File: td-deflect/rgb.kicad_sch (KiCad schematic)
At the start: 83 parts, among them J16 Conn_01x06_Male, J17 Conn_01x06_Male, J5 DB15_Female_HighDensity, J7 Conn_01x08_Male, Q14 BC847, Q15 BC847, Q16 BC847, SW1 SW_DIP_x04, U11 24LC08, U18 M51387P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

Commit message: more updates
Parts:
- removed C59: 0.1uF, Capacitor_SMD:C_0805_2012Metric_Pad1.15x1.40mm_HandSolder, symbol Device:C
- removed C60: 220uF, Capacitor_THT:CP_Radial_D8.0mm_P3.50mm, symbol Device:CP
- removed D6, D7, D8: BAT54S, Package_TO_SOT_SMD:SOT-23, symbol Diode:BAT54S
- removed Q14, Q15, Q16: BC847, Package_TO_SOT_SMD:SOT-23, symbol Transistor_BJT:BC847
- removed R56, R57: 1.5k, Resistor_SMD:R_0805_2012Metric_Pad1.15x1.40mm_HandSolder, symbol Device:R
- removed R64, R68: 560, Resistor_SMD:R_0805_2012Metric_Pad1.15x1.40mm_HandSolder, symbol Device:R
- removed R65, R66, R67, R82, R95: 220, Resistor_SMD:R_0805_2012Metric_Pad1.15x1.40mm_HandSolder, symbol Device:R
- removed R69, R73, R74, R75: 47k, Resistor_SMD:R_0805_2012Metric_Pad1.15x1.40mm_HandSolder, symbol Device:R
- removed R70, R71, R72, R76, R77, R78: 1k, Resistor_SMD:R_0805_2012Metric_Pad1.15x1.40mm_HandSolder, symbol Device:R
- removed R79, R80, R81: 47, Resistor_SMD:R_0805_2012Metric_Pad1.15x1.40mm_HandSolder, symbol Device:R
- removed R83, R84, R85: 470, Resistor_SMD:R_0805_2012Metric_Pad1.15x1.40mm_HandSolder, symbol Device:R
- removed R94: 33k, Resistor_SMD:R_0805_2012Metric_Pad1.15x1.40mm_HandSolder, symbol Device:R
- removed RV2, RV4, RV5: 2.7k, Potentiometer_THT:Potentiometer_Bourns_3386P_Vertical, symbol Device:R_POT
- removed RV3: 2k, Potentiometer_THT:Potentiometer_Bourns_3386P_Vertical, symbol Device:R_POT
- removed RV6, RV7, RV8, RV9: 1k, Potentiometer_THT:Potentiometer_Bourns_3386P_Vertical, symbol Device:R_POT
- removed U18: M51387P, td-deflect:DIP-30_600_ELL, symbol td-deflect:M51387P
- added J1: Conn_01x10_Socket, symbol Connector:Conn_01x10_Pin
- added U18: LM1205, Package_DIP:DIP-28_W15.24mm, symbol td-crt:LM1205
- added U26, U27: MCP4728, Package_SO:MSOP-10_3x3mm_P0.5mm, symbol Analog_DAC:MCP4728
- added U29: MCP6001U, Package_SO:SOIC-8_3.9x4.9mm_P1.27mm, symbol Amplifier_Operational:MCP6001U
- C47: value 0.1uF -> 10uF; Digikey 1276-1099-1-ND -> (none)
- C48, C49: value 47uF -> 10uF; footprint Capacitor_SMD:C_1206_3216Metric_Pad1.42x1.75mm_HandSolder -> Capacitor_SMD:C_0805_2012Metric_Pad1.15x1.40mm_HandSolder; Digikey 1276-3064-1-ND -> (none); Voltage 6.3V -> (none)
- C50: value 47uF -> 0.1uF; footprint Capacitor_SMD:C_1206_3216Metric_Pad1.42x1.75mm_HandSolder -> Capacitor_SMD:C_0805_2012Metric_Pad1.15x1.40mm_HandSolder; Digikey 1276-3064-1-ND -> (none); Voltage 6.3V -> (none)
- C51, C52: Digikey 1276-1099-1-ND -> (none)
- C53, C55: value 2.2uF -> C; Digikey 1276-2953-1-ND -> (none); Voltage 25V -> (none)
- C54: value 0.1uF -> C; Digikey 1276-1099-1-ND -> (none)
- C56: value 2.2uF -> 0.1uF; Digikey 1276-2953-1-ND -> (none); Voltage 25V -> (none)
- R51: value 6.8k -> 30; Digikey 311-6.80KCRCT-ND -> (none)
- R52: value 2.7k -> 30; Digikey 311-2.70KCRCT-ND -> (none)
- R53: value 0 -> 30; Digikey 311-0.0ARCT-ND -> (none)
- R54: value 2.2k -> 100; Digikey 311-2.20KCRCT-ND -> (none)
- R55: value 1.5k -> 100; Digikey 311-1.50KCRCT-ND -> (none)
- R58, R61: value 6.8k -> R; Digikey 311-6.80KCRCT-ND -> (none)
- R59, R62: value 2.7k -> R; Digikey 311-2.70KCRCT-ND -> (none)
- R60: value 560 -> R; Digikey 311-560CRCT-ND -> (none)
- R63: value 0 -> R; Digikey 311-0.0ARCT-ND -> (none)
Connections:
- net +12V: now also U18.11 (VCC), U18.22 (VCC), U18.23 (VCC), U18.25 (VCC), U18.3 (VCC); no longer R51.1, R53.1, R58.1, R61.1
- net +3V3: now also U26.1 (VDD), U27.1 (VDD)
- net GND: now also C50.1, C51.1, C52.1, J1.10 (Pin_10), U18.21 (GROUND), U18.24 (GROUND), U18.7 (GROUND), U26.10 (VSS), U27.10 (VSS), U29.2 (V-); no longer C47.2, C51.2, C52.2, R52.2, R54.2, R59.2, R60.2, R62.2, R63.2
- net blue_vga: now also R53.1
- net green_vga: now also R52.1
- net red_vga: now also R51.1; no longer R55.2
- net uc_blank: now also R54.1
- net at U20.4: now also R55.1
- net +3.3VA: now reaches C56.1
- net +3.3VA: now also J1.1 (Pin_1), U29.5 (V+)
- net at C55.1: now also R60.2, R63.2, U18.19 (GREEN_CUT-OFF_ADJ)
- net at C53.1: now also R61.2, R62.2, U18.16 (BLUE_CUT-OFF_ADJ)
- net at C48.1: now also R52.2
- net at C49.2: now also U18.9 (BLUE_VIDEO_IN)
- net at C49.1: now also R53.2
- net at C50.2: now also U18.5 (RED_CLAMP_CAP)
- net at R51.2: now also C47.1
- net bbias: now reaches R62.1
- net bbias: now also J1.4 (Pin_4), U26.8 (VOUTC)
- net at R58.2: now also C54.1, R59.2, U18.27 (RED_CUT-OFF_ADJ)
- net rbias: now reaches R59.1
- net rbias: now also J1.2 (Pin_2), U26.6 (VOUTA)
- net gbias: now reaches R63.1
- net gbias: now also J1.3 (Pin_3), U26.7 (VOUTB)
- net at R86.2: now also U18.26 (RED_VIDEO_OUT)
- net at R87.2: now also U18.20 (GREEN_VIDEO_OUT)
- net at R88.2: now also U18.17 (BLUE_VIDEO_OUT)
- new net: C52.2, U18.10 (BLUE_CLAMP_CAP)
- new net: R54.2, U18.13 (~{BLANK_GATE})
- new net: R55.2, U18.14 (~{CLAMP_GATE})
- new net: C47.2, U18.4 (RED_VIDEO_IN)
- new net: C48.2, U18.6 (GREEN_VIDEO_IN)
- new net: C51.2, U18.8 (GREEN_CLAMP_CAP)
- new net: R58.1, R60.1, R61.1, U29.3 (-), U29.4
- new net BIAS_LOAD: U26.4 (~{LDAC})
- new net GAIN_LOAD: U27.4 (~{LDAC})
- new net SCL: U26.2 (SCL), U27.2 (SCL)
- new net SDA: U26.3 (SDA), U27.3 (SDA)
- new net bgain: J1.8 (Pin_8), U18.15 (BLUE_DRIVE_ADJ), U27.8 (VOUTC)
- new net ggain: J1.7 (Pin_7), U18.18 (GREEN_DRIVE_ADJ), U27.7 (VOUTB)
- new net globalbias: J1.5 (Pin_5), U26.9 (VOUTD), U29.1 (+)
- new net globalgain: J1.9 (Pin_9), U18.12 (CONTRAST), U27.9 (VOUTD)
- new net rgain: J1.6 (Pin_6), U18.28 (RED_DRIVE_ADJ), U27.6 (VOUTA)
- no-connect marks 8 -> 7
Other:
- note removed: "todo: replace this chip entirely lol"
- moved on the sheet: R88

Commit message: even more updates
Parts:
- J1: footprint (none) -> Connector_JST:JST_XH_B10B-XH-A_1x10_P2.50mm_Vertical
- SW1: footprint Button_Switch_THT:SW_DIP_SPSTx04_Slide_9.78x12.34mm_W7.62mm_P2.54mm -> Button_Switch_SMD:SW_DIP_SPSTx04_Slide_Omron_A6S-410x_W8.9mm_P2.54mm; Digikey CT2064-ND -> (none)
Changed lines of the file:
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@@
       (effects (font (size 1.27 1.27)))
     )
-    (property "Footprint" "Button_Switch_THT:SW_DIP_SPSTx04_Slide_9.78x12.34mm_W7.62mm_P2.54mm" (at 265.43 137.16 0)
+    (property "Footprint" "Button_Switch_SMD:SW_DIP_SPSTx04_Slide_Omron_A6S-410x_W8.9mm_P2.54mm" (at 265.43 137.16 0)
       (effects (font (size 1.27 1.27)) hide)
     )
@@
       (effects (font (size 1.27 1.27)) hide)
     )
-    (property "Digikey" " CT2064-ND " (at 265.43 137.16 0)
+    (property "Digikey" "" (at 265.43 137.16 0)
       (effects (font (size 1.27 1.27)) hide)
     )
@@
       (effects (font (size 1.27 1.27)))
     )
-    (property "Footprint" "" (at 170.18 172.72 0)
-      (effects (font (size 1.27 1.27)) hide)
-    )
+    (property "Footprint" "Connector_JST:JST_XH_B10B-XH-A_1x10_P2.50mm_Vertical" (at 170.18 172.72 0)
+      (effects (font (size 1.27 1.27)) hide)
+    )

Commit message: small bugfix
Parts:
- added C90: 0.1uF, symbol Device:C
- added C91, C92: 0.1uF, Capacitor_SMD:C_0805_2012Metric_Pad1.15x1.40mm_HandSolder, symbol Device:C
- added R111: 30, symbol Device:R
- C53, C54, C55: value C -> 0.1uF
- R58, R59, R60, R61, R62, R63: value R -> 10k
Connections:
- net +12V: now also C91.1
- net +3.3VA: now also U26.1 (VDD), U27.1 (VDD), C92.1
- net +3V3: no longer U26.1 (VDD), U27.1 (VDD)
- net GND: now also C91.2, C92.2
- net at U18.1 (CONTRAST_CAP): now also C90.1
- net at U18.2 (CONTRAST_CAP): now also R111.2
- new net: C90.2, R111.1

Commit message: switch to new 0805 footprint
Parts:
- C47, C48, C49, C50, C51, C52, C53, C54, C55, C56, C57, C58, C91, C92: footprint Capacitor_SMD:C_0805_2012Metric_Pad1.15x1.40mm_HandSolder -> Capacitor_SMD:C_0805_2012Metric_Pad1.18x1.45mm_HandSolder
- C90: footprint (none) -> Capacitor_SMD:C_0805_2012Metric_Pad1.18x1.45mm_HandSolder
- R111: footprint (none) -> Resistor_SMD:R_0805_2012Metric_Pad1.20x1.40mm_HandSolder
- R51, R52, R53, R54, R55, R58, R59, R60, R61, R62, R63, R86, R87, R88, R89, R90, R91, R92, R93: footprint Resistor_SMD:R_0805_2012Metric_Pad1.15x1.40mm_HandSolder -> Resistor_SMD:R_0805_2012Metric_Pad1.20x1.40mm_HandSolder

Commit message: external rgb
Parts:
- removed C47, C48, C49: 10uF, Capacitor_SMD:C_0805_2012Metric_Pad1.18x1.45mm_HandSolder, symbol Device:C
- removed C50, C51, C52, C53, C54, C55, C56, C58, C90, C91, C92: 0.1uF, Capacitor_SMD:C_0805_2012Metric_Pad1.18x1.45mm_HandSolder, symbol Device:C
- removed C57: 1uF, Capacitor_SMD:C_0805_2012Metric_Pad1.18x1.45mm_HandSolder, symbol Device:C
- removed J1: Conn_01x10_Socket, Connector_JST:JST_XH_B10B-XH-A_1x10_P2.50mm_Vertical, symbol Connector:Conn_01x10_Pin
- removed J16: Conn_01x06_Male, Connector_JST:JST_EH_B6B-EH-A_1x06_P2.50mm_Vertical, symbol Connector:Conn_01x06_Male
- removed J17: Conn_01x06_Male, Connector_JST:JST_XH_B6B-XH-A_1x06_P2.50mm_Vertical, symbol Connector:Conn_01x06_Male
- removed J5: DB15_Female_HighDensity, Connector_Dsub:DSUB-15-HD_Female_Horizontal_P2.29x1.98mm_EdgePinOffset3.03mm_Housed_MountingHolesOffset4.94mm, symbol Connector:DB15_Female_HighDensity
- removed J7: Conn_01x08_Male, Connector_JST:JST_PH_B8B-PH-K_1x08_P2.00mm_Vertical, symbol Connector:Conn_01x08_Male
- removed R111, R51, R52, R53: 30, Resistor_SMD:R_0805_2012Metric_Pad1.20x1.40mm_HandSolder, symbol Device:R
- removed R54, R55: 100, Resistor_SMD:R_0805_2012Metric_Pad1.20x1.40mm_HandSolder, symbol Device:R
- removed R58, R59, R60, R61, R62, R63, R89: 10k, Resistor_SMD:R_0805_2012Metric_Pad1.20x1.40mm_HandSolder, symbol Device:R
- removed R86, R87, R88: 47, Resistor_SMD:R_0805_2012Metric_Pad1.20x1.40mm_HandSolder, symbol Device:R
- removed R90, R91, R92, R93: 75, Resistor_SMD:R_0805_2012Metric_Pad1.20x1.40mm_HandSolder, symbol Device:R
- removed RV10: 10k, Potentiometer_THT:Potentiometer_Bourns_3386P_Vertical, symbol Device:R_POT
- removed SW1: SW_DIP_x04, Button_Switch_SMD:SW_DIP_SPSTx04_Slide_Omron_A6S-410x_W8.9mm_P2.54mm, symbol Switch:SW_DIP_x04
- removed U11: 24LC08, Package_SO:SOIC-8_3.9x4.9mm_P1.27mm, symbol Memory_EEPROM:24LC08
- removed U18: LM1205, Package_DIP:DIP-28_W15.24mm, symbol td-crt:LM1205
- removed U19: LMH1980, Package_SO:VSSOP-10_3x3mm_P0.5mm, symbol td-deflect:LMH1980
- removed U20: 74LVC1GU04DRLR, Package_TO_SOT_SMD:SOT-553, symbol 74xGxx:74LVC1GU04DRL
- removed U26, U27: MCP4728, Package_SO:MSOP-10_3x3mm_P0.5mm, symbol Analog_DAC:MCP4728
- removed U29: MCP6001U, Package_SO:SOIC-8_3.9x4.9mm_P1.27mm, symbol Amplifier_Operational:MCP6001U
- added J2: Conn_01x07_Male, Connector_JST:JST_XH_B7B-XH-A_1x07_P2.50mm_Vertical, symbol Connector:Conn_01x07_Male
- added J3: Conn_01x05_Pin, Connector_JST:JST_XH_B5B-XH-A_1x05_P2.50mm_Vertical, symbol Connector:Conn_01x05_Pin
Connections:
- net +12V: now also J2.2 (Pin_2)
- net BIAS_LOAD: now also J3.3 (Pin_3)
- net GAIN_LOAD: now also J3.4 (Pin_4)
- net GND: now also J2.1 (Pin_1), J3.5 (Pin_5)
- net SCL: now also J3.1 (Pin_1)
- net SDA: now also J3.2 (Pin_2)
- new net LM1205_BLANK: J2.7 (Pin_7)
- new net SEP_HSYNC: J2.4 (Pin_4)
- new net SEP_OE: J2.5 (Pin_5)
- new net SEP_VSYNC: J2.6 (Pin_6)
- new net VGA_VSYNC: J2.3 (Pin_3)
- no-connect marks 7 -> 0

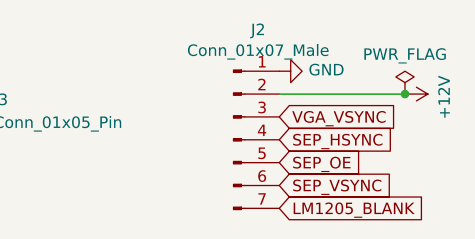
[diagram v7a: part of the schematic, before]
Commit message: fix remaining erc errors
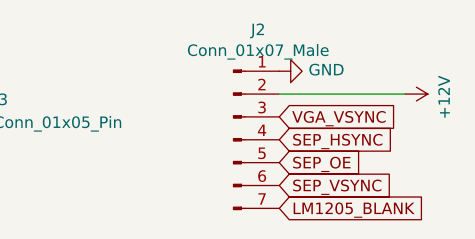
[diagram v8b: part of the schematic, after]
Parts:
- J2: symbol Connector:Conn_01x07_Male -> Connector:Conn_01x07_Pin
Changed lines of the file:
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@@
 (kicad_sch (version 20230121) (generator eeschema)
   (paper "A4")
-  (junction (at 162.56 107.95) (diameter 0) (color 0 0 0 0)
-  )
   (wire (pts (xy 162.56 107.95) (xy 148.59 107.95))
     (stroke (width 0) (type default))
@@
     )
   )
-  (symbol (lib_id "power:PWR_FLAG") (at 162.56 107.95 0) (unit 1)
-    (in_bom yes) (on_board yes) (dnp no)
-    (property "Reference" "#FLG0101" (at 162.56 106.045 0)
-      (effects (font (size 1.27 1.27)) hide)
-    )
-    (property "Value" "PWR_FLAG" (at 162.56 103.5558 0)
-      (effects (font (size 1.27 1.27)))
-    )
-    (property "Footprint" "" (at 162.56 107.95 0)
-      (effects (font (size 1.27 1.27)) hide)
-    )
-    (property "Datasheet" "~" (at 162.56 107.95 0)
-      (effects (font (size 1.27 1.27)) hide)
-    )
-    (pin "1")
-    (instances
-      (project "td-rgbinput-lm1205"
-        (path "/3efa2ece-8f3f-4a8c-96e9-6ab3ec6f1f70"
-          (reference "#FLG0101") (unit 1)
-        )
-      )
-      (project "td-deflect"
-        (path "/55a1a5e1-4d11-4c3e-b2b4-b9d50ddc5f9d/00000000-0000-0000-0000-00005dbce206"
-          (reference "#FLG01") (unit 1)
-        )
-      )
-    )
-  )
   (symbol (lib_id "Connector:Conn_01x05_Pin") (at 115.57 109.22 0) (mirror y) (unit 1)
     (in_bom yes) (on_board yes) (dnp no) (fields_autoplaced)
@@
     )
   )
-  (symbol (lib_id "Connector:Conn_01x07_Male") (at 143.51 113.03 0) (unit 1)
+  (symbol (lib_id "Connector:Conn_01x07_Pin") (at 143.51 113.03 0) (unit 1)
     (in_bom yes) (on_board yes) (dnp no)
     (property "Reference" "J2" (at 146.2532 100.8126 0)
